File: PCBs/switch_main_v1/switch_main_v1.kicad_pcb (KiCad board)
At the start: 2 copper layers, 166 parts, among them IC1001 TJA1055T_3_2Z, J1101 76825-0004, J1102 PJ-002AH, J901 TMJG46945AENL, Q1101 DMTH6016LPSQ-13, U1101 TVS2701DRBR, U1102 MPQ5850GJ-AEC1-Z, U201 SJA1105QELY, U301 M24256X-FCU6T_VF, U302 STM32H573RIVx, U401 TPS16416DRCR, U402 LMR34206SC5QRNXRQ1, U403 LT8692SIV-PBF, U501 DP83867CSRGZR, U601 DP83867CSRGZR, U701 DP83867CSRGZR, U801 DP83867CSRGZR, Y501 ECS-250-18-36B2-CTY-TR, Y601 ECS-250-18-36B2-CTY-TR, Y701 ECS-250-18-36B2-CTY-TR, Y801 ECS-250-18-36B2-CTY-TR

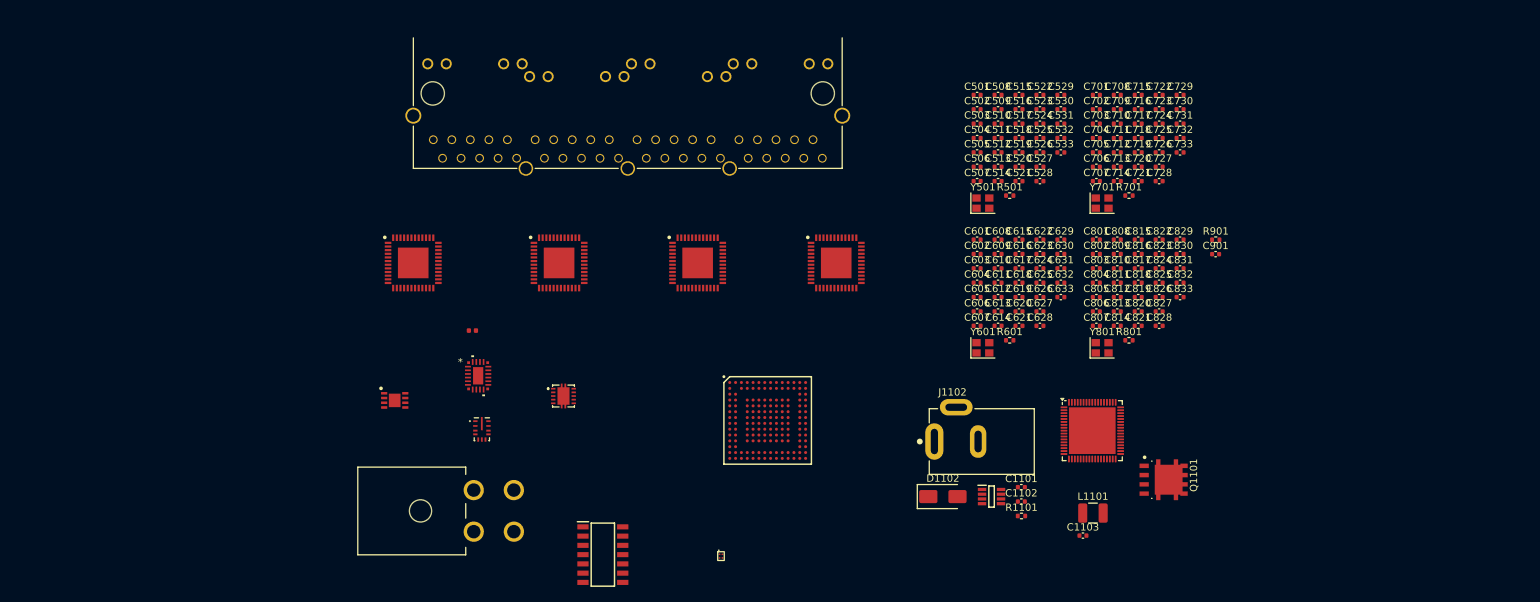
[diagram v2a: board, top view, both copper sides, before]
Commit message: GbE part of schematic done
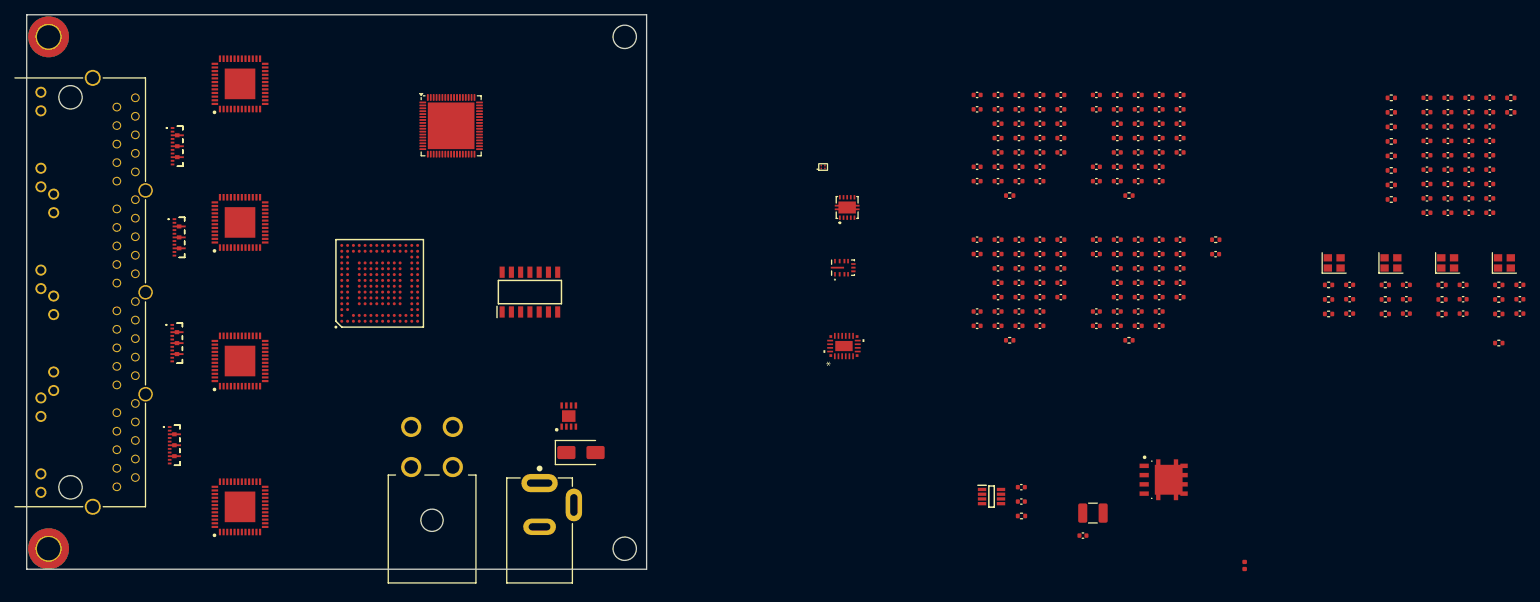
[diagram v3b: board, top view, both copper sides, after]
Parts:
- added C201: 100n, Capacitor_SMD:C_0402_1005Metric, F.Cu at (262.0, 66.4)
- added C202: 100n, Capacitor_SMD:C_0402_1005Metric, F.Cu at (262.0, 68.3)
- added C204: 100n, Capacitor_SMD:C_0402_1005Metric, F.Cu at (262.0, 70.3)
- added C205: 100n, Capacitor_SMD:C_0402_1005Metric, F.Cu at (262.0, 72.3)
- added C206: 100n, Capacitor_SMD:C_0402_1005Metric, F.Cu at (262.0, 74.2)
- added C207: 100n, Capacitor_SMD:C_0402_1005Metric, F.Cu at (262.0, 76.2)
- added C208: 100n, Capacitor_SMD:C_0402_1005Metric, F.Cu at (262.0, 78.2)
- added C209: 100n, Capacitor_SMD:C_0402_1005Metric, F.Cu at (262.0, 80.2)
- added C210: 100n, Capacitor_SMD:C_0402_1005Metric, F.Cu at (262.0, 82.1)
- added C211: 100n, Capacitor_SMD:C_0402_1005Metric, F.Cu at (264.9, 66.4)
- added C212: 100n, Capacitor_SMD:C_0402_1005Metric, F.Cu at (264.9, 68.3)
- added C213: 100n, Capacitor_SMD:C_0402_1005Metric, F.Cu at (264.9, 70.3)
- added C214: 1u, Capacitor_SMD:C_0402_1005Metric, F.Cu at (264.9, 72.3)
- added C215: 1u, Capacitor_SMD:C_0402_1005Metric, F.Cu at (264.9, 74.2)
- added C216: 100n, Capacitor_SMD:C_0402_1005Metric, F.Cu at (264.9, 76.2)
- added C217: 1u, Capacitor_SMD:C_0402_1005Metric, F.Cu at (264.9, 78.2)
- added C218: 1u, Capacitor_SMD:C_0402_1005Metric, F.Cu at (264.9, 80.2)
- added C219: 1u, Capacitor_SMD:C_0402_1005Metric, F.Cu at (264.9, 82.1)
- added C220: 100n, Capacitor_SMD:C_0402_1005Metric, F.Cu at (267.7, 66.4)
- added C221: 1u, Capacitor_SMD:C_0402_1005Metric, F.Cu at (267.7, 68.3)
- added C222: 10u, Capacitor_SMD:C_0402_1005Metric, F.Cu at (267.7, 70.3)
- added C224: 1u, Capacitor_SMD:C_0402_1005Metric, F.Cu at (267.7, 72.3)
- added C225: 1u, Capacitor_SMD:C_0402_1005Metric, F.Cu at (267.7, 74.2)
- added C227: 10u, Capacitor_SMD:C_0402_1005Metric, F.Cu at (267.7, 76.2)
- added C230: 10u, Capacitor_SMD:C_0402_1005Metric, F.Cu at (267.7, 78.2)
- added C231: 100p, Capacitor_SMD:C_0402_1005Metric, F.Cu at (267.7, 80.2)
- added C232: 100n, Capacitor_SMD:C_0402_1005Metric, F.Cu at (267.7, 82.1)
- added C233: 100n, Capacitor_SMD:C_0402_1005Metric, F.Cu at (270.6, 66.4)
- added C234: 100n, Capacitor_SMD:C_0402_1005Metric, F.Cu at (270.6, 68.3)
- added C235: 100n, Capacitor_SMD:C_0402_1005Metric, F.Cu at (270.6, 70.3)
- added C236: 100n, Capacitor_SMD:C_0402_1005Metric, F.Cu at (270.6, 72.3)
- added C237: 100n, Capacitor_SMD:C_0402_1005Metric, F.Cu at (270.6, 74.2)
- added C238: 1u, Capacitor_SMD:C_0402_1005Metric, F.Cu at (270.6, 76.2)
- added C239: 1u, Capacitor_SMD:C_0402_1005Metric, F.Cu at (270.6, 78.2)
- added C240: 100n, Capacitor_SMD:C_0402_1005Metric, F.Cu at (270.6, 80.2)
- added C241: 100n, Capacitor_SMD:C_0402_1005Metric, F.Cu at (270.6, 82.1)
- added D901: ESD8708MUTAG, switch_footprints:ESD8708MUTAG, F.Cu at (90.7, 73.0)
- added D902: ESD8708MUTAG, switch_footprints:ESD8708MUTAG, F.Cu at (90.9, 85.5)
- added D903: ESD8708MUTAG, switch_footprints:ESD8708MUTAG, F.Cu at (90.6, 100.0)
- added D904: ESD8708MUTAG, switch_footprints:ESD8708MUTAG, F.Cu at (90.3, 114.0)
- added H101: MountingHole_Pad, MountingHole:MountingHole_3.2mm_M3_DIN965_Pad_TopBottom, F.Cu at (73.0, 128.2)
- added H102: MountingHole_Pad, MountingHole:MountingHole_3.2mm_M3_DIN965_Pad_TopBottom, F.Cu at (73.0, 58.0)
- added H103: MountingHole, MountingHole:MountingHole_3.2mm_M3_DIN965, F.Cu at (152.0, 58.0)
- added H104: MountingHole, MountingHole:MountingHole_3.2mm_M3_DIN965, F.Cu at (152.0, 128.2)
- added R201: 1k, Resistor_SMD:R_0402_1005Metric, F.Cu at (273.5, 66.4)
- added R202: 2k2, Resistor_SMD:R_0402_1005Metric, F.Cu at (273.5, 68.4)
- added R301: 1k5, Resistor_SMD:R_0402_1005Metric, F.Cu at (271.9, 100.0)
- added R502: 27k, Resistor_SMD:R_0402_1005Metric, F.Cu at (248.5, 92.0)
- added R503: 2k2, Resistor_SMD:R_0402_1005Metric, F.Cu at (248.5, 94.0)
- added R504: 2k2, Resistor_SMD:R_0402_1005Metric, F.Cu at (248.5, 96.0)
- added R602: 27k, Resistor_SMD:R_0402_1005Metric, F.Cu at (256.3, 92.0)
- added R603: 2k2, Resistor_SMD:R_0402_1005Metric, F.Cu at (256.3, 94.0)
- added R604: 2k2, Resistor_SMD:R_0402_1005Metric, F.Cu at (256.3, 96.0)
- added R702: 27k, Resistor_SMD:R_0402_1005Metric, F.Cu at (264.1, 92.0)
- added R703: 2k2, Resistor_SMD:R_0402_1005Metric, F.Cu at (264.1, 94.0)
- added R704: 2k2, Resistor_SMD:R_0402_1005Metric, F.Cu at (264.1, 96.0)
- added R802: 27k, Resistor_SMD:R_0402_1005Metric, F.Cu at (271.9, 92.0)
- added R803: 2k2, Resistor_SMD:R_0402_1005Metric, F.Cu at (271.9, 94.0)
- added R804: 2k2, Resistor_SMD:R_0402_1005Metric, F.Cu at (271.9, 96.0)
- added R902: 470R, Resistor_SMD:R_0402_1005Metric, F.Cu at (257.1, 66.4)
- added R903: 470R, Resistor_SMD:R_0402_1005Metric, F.Cu at (257.1, 68.4)
- added R904: 470R, Resistor_SMD:R_0402_1005Metric, F.Cu at (257.1, 70.3)
- added R905: 470R, Resistor_SMD:R_0402_1005Metric, F.Cu at (257.1, 72.3)
- added R906: 470R, Resistor_SMD:R_0402_1005Metric, F.Cu at (257.1, 74.3)
- added R907: 470R, Resistor_SMD:R_0402_1005Metric, F.Cu at (257.1, 76.3)
- added R908: 470R, Resistor_SMD:R_0402_1005Metric, F.Cu at (257.1, 78.3)
- added R909: 470R, Resistor_SMD:R_0402_1005Metric, F.Cu at (257.1, 80.3)
- C901: value C_Small -> 4n7
- R901: value R_Small -> 1M
- moved D1101 110.7 mm to (237.0, 130.5), turned to 90 degrees
- moved U302 97.3 mm to (128.2, 70.2)
- moved U801 85.4 mm to (99.2, 64.5), turned to 90 degrees
- moved J901 73.0 mm to (82.5, 93.0), turned to -90 degrees
- moved U601 63.0 mm to (99.2, 83.5), turned to 90 degrees
- moved C603 58.9 mm to (259.2, 92.0)
- moved C604 58.9 mm to (259.2, 94.0)
- moved C605 58.9 mm to (259.2, 96.0)
- moved C803 58.1 mm to (274.7, 92.0)
- moved C804 58.1 mm to (274.7, 94.0)
- moved C805 58.1 mm to (274.7, 96.0)
- moved Y601 57.1 mm to (257.1, 89.0)
- moved U201 56.4 mm to (118.4, 91.8), turned to 90 degrees
- moved Y801 56.4 mm to (272.6, 89.0)
- moved C503 55.7 mm to (251.4, 92.0)
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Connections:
- net /Switch/SPI.CS renamed /SPI3.CS
- net /Switch/SPI.MISO renamed /SPI3.MISO
- net /Switch/SPI.MOSI renamed /SPI3.MOSI
- net /Switch/SPI.SCK renamed /SPI3.SCK
- C503 pad 2: /PHY_1_CLK -> GND
- C504 pad 1: /PHY 1/XI -> /PHY 1/XO
- C505 pad 1: /PHY 1/XO -> /PHY 1/XI
- C505 pad 2: GND -> /PHY_1_CLK
- C603 pad 2: /PHY_2_CLK -> GND
- C604 pad 1: /PHY 2/XI -> /PHY 2/XO
- C605 pad 1: /PHY 2/XO -> /PHY 2/XI
- C605 pad 2: GND -> /PHY_2_CLK
- C703 pad 2: /PHY_3_CLK -> GND
- C704 pad 1: /PHY 3/XI -> /PHY 3/XO
- C705 pad 1: /PHY 3/XO -> /PHY 3/XI
- C705 pad 2: GND -> /PHY_3_CLK
- C803 pad 2: /PHY_4_CLK -> GND
- C804 pad 1: /PHY 4/XI -> /PHY 4/XO
- C805 pad 1: /PHY 4/XO -> /PHY 4/XI
- C805 pad 2: GND -> /PHY_4_CLK
- J901 pad 11A: unconnected-(J901-ANODE-Pad11A) -> /RJ45s/LED_G_1_A
- J901 pad 11B: unconnected-(J901-ANODE-Pad11B) -> /RJ45s/LED_G_2_A
- J901 pad 11C: unconnected-(J901-ANODE-Pad11C) -> /RJ45s/LED_G_3_A
- J901 pad 11D: unconnected-(J901-ANODE-Pad11D) -> /RJ45s/LED_G_4_A
- J901 pad 12A: unconnected-(J901-CATHODE-Pad12A) -> GND
- J901 pad 12B: unconnected-(J901-CATHODE-Pad12B) -> GND
- J901 pad 12C: unconnected-(J901-CATHODE-Pad12C) -> GND
- J901 pad 12D: unconnected-(J901-CATHODE-Pad12D) -> GND
- J901 pad 13A: unconnected-(J901-ANODE-Pad13A) -> /RJ45s/LED_Y_1_A
- J901 pad 13B: unconnected-(J901-ANODE-Pad13B) -> /RJ45s/LED_Y_2_A
- J901 pad 13C: unconnected-(J901-ANODE-Pad13C) -> /RJ45s/LED_Y_3_A
- J901 pad 13D: unconnected-(J901-ANODE-Pad13D) -> /RJ45s/LED_Y_4_A
- J901 pad 14A: unconnected-(J901-CATHODE-Pad14A) -> GND
- J901 pad 14B: unconnected-(J901-CATHODE-Pad14B) -> GND
- J901 pad 14C: unconnected-(J901-CATHODE-Pad14C) -> GND
- J901 pad 14D: unconnected-(J901-CATHODE-Pad14D) -> GND
- U201 pad J1: unconnected-(U201B-VDDA_PLL-PadJ1) -> +1V2
- U201 pad K1: unconnected-(U201B-VDDA_OSC-PadK1) -> +1V2
- U201 pad K2: unconnected-(U201A-OSC_IN-PadK2) -> /Switch/OSC_IN
- U201 pad P3: /Switch/RST -> /ETHERNET_RST
- U501 pad 20: unconnected-(U501-JTAG_CLK-Pad20) -> GND
- U501 pad 22: unconnected-(U501-JTAG_TMS-Pad22) -> +2V5
- U501 pad 23: unconnected-(U501-JTAG_TDI-Pad23) -> +2V5
- U501 pad 43: unconnected-(U501-RESET_N-Pad43) -> /ETHERNET_RST
- U501 pad 44: unconnected-(U501-INT/PWDN-Pad44) -> /PHY_INT
- U501 pad 45: unconnected-(U501-LED_2-Pad45) -> /LED_Y_1
- U501 pad 47: unconnected-(U501-LED_0-Pad47) -> /LED_G_1
- U601 pad 20: unconnected-(U601-JTAG_CLK-Pad20) -> GND
- U601 pad 22: unconnected-(U601-JTAG_TMS-Pad22) -> +2V5
- U601 pad 23: unconnected-(U601-JTAG_TDI-Pad23) -> +2V5
- U601 pad 43: unconnected-(U601-RESET_N-Pad43) -> /ETHERNET_RST
- U601 pad 44: unconnected-(U601-INT/PWDN-Pad44) -> /PHY_INT
- U601 pad 45: unconnected-(U601-LED_2-Pad45) -> /LED_Y_2
- U601 pad 47: unconnected-(U601-LED_0-Pad47) -> /LED_G_2
- U701 pad 20: unconnected-(U701-JTAG_CLK-Pad20) -> GND
- U701 pad 22: unconnected-(U701-JTAG_TMS-Pad22) -> +2V5
- U701 pad 23: unconnected-(U701-JTAG_TDI-Pad23) -> +2V5
- U701 pad 43: unconnected-(U701-RESET_N-Pad43) -> /ETHERNET_RST
- U701 pad 44: unconnected-(U701-INT/PWDN-Pad44) -> /PHY_INT
- U701 pad 45: unconnected-(U701-LED_2-Pad45) -> /LED_Y_3
- U701 pad 47: unconnected-(U701-LED_0-Pad47) -> /LED_G_3
- U801 pad 20: unconnected-(U801-JTAG_CLK-Pad20) -> GND
- U801 pad 22: unconnected-(U801-JTAG_TMS-Pad22) -> +2V5
- U801 pad 23: unconnected-(U801-JTAG_TDI-Pad23) -> +2V5
- U801 pad 43: unconnected-(U801-RESET_N-Pad43) -> /ETHERNET_RST
- U801 pad 44: unconnected-(U801-INT/PWDN-Pad44) -> /PHY_INT
- U801 pad 45: unconnected-(U801-LED_2-Pad45) -> /LED_Y_4
- U801 pad 47: unconnected-(U801-LED_0-Pad47) -> /LED_G_4
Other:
- board outline added: 85 x 76 mm

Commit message: Changed MCU to STM32H573IIK3Q
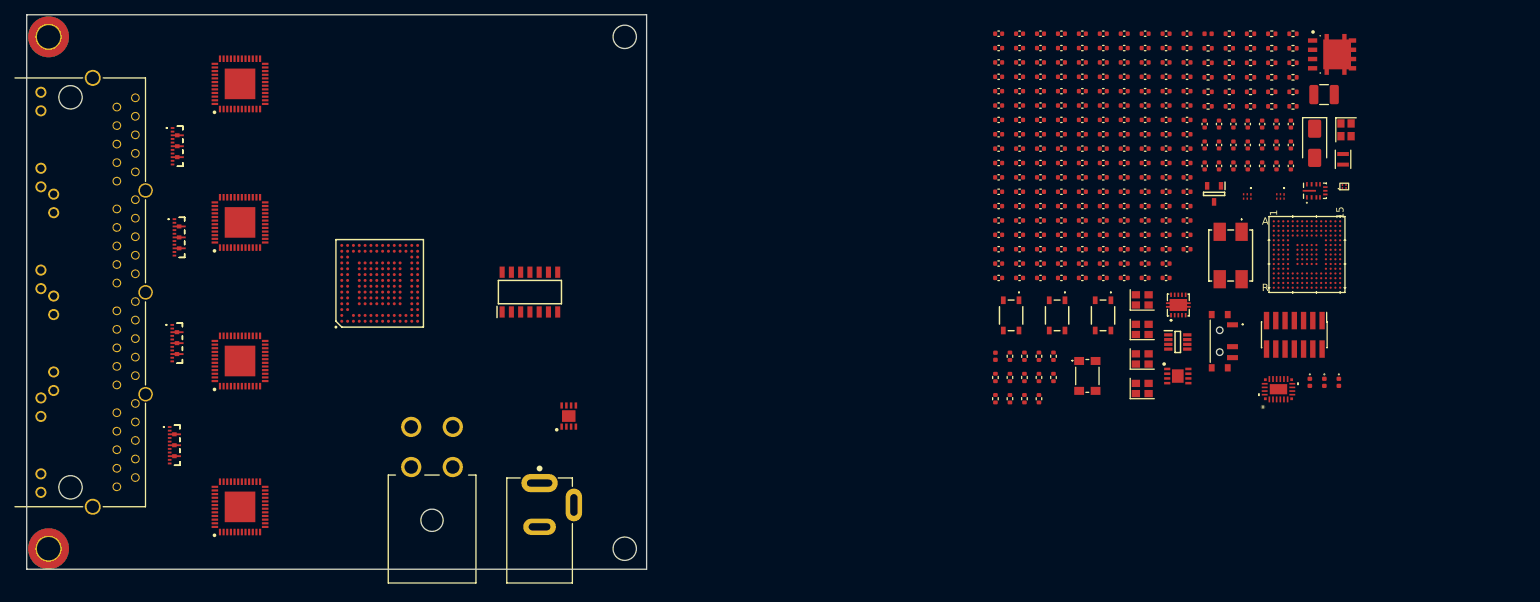
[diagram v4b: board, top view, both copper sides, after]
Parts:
- added C301: 220p, Capacitor_SMD:C_0402_1005Metric, F.Cu at (231.5, 70.0)
- added C302: 100n, Capacitor_SMD:C_0402_1005Metric, F.Cu at (233.5, 70.0)
- added C303: 1u, Capacitor_SMD:C_0402_1005Metric, F.Cu at (235.5, 70.0)
- added C304: 4u7, Capacitor_SMD:C_0402_1005Metric, F.Cu at (237.4, 70.0)
- added C305: 10u, Capacitor_SMD:C_0402_1005Metric, F.Cu at (239.4, 70.0)
- added C306: 100n, Capacitor_SMD:C_0402_1005Metric, F.Cu at (241.4, 70.0)
- added C307: 10n, Capacitor_SMD:C_0402_1005Metric, F.Cu at (243.3, 70.0)
- added C308: 10n, Capacitor_SMD:C_0402_1005Metric, F.Cu at (231.5, 72.8)
- added C309: 4u7, Capacitor_SMD:C_0402_1005Metric, F.Cu at (233.5, 72.8)
- added C310: 100n, Capacitor_SMD:C_0402_1005Metric, F.Cu at (235.5, 72.8)
- added C311: 10n, Capacitor_SMD:C_0402_1005Metric, F.Cu at (237.4, 72.8)
- added C312: 6p, Capacitor_SMD:C_0402_1005Metric, F.Cu at (239.4, 72.8)
- added C313: 4u7, Capacitor_SMD:C_0402_1005Metric, F.Cu at (241.4, 72.8)
- added C314: 100n, Capacitor_SMD:C_0402_1005Metric, F.Cu at (243.3, 72.8)
- added C315: 6p, Capacitor_SMD:C_0402_1005Metric, F.Cu at (231.5, 75.7)
- added C316: 100n, Capacitor_SMD:C_0402_1005Metric, F.Cu at (209.0, 57.6)
- added C317: 100n, Capacitor_SMD:C_0402_1005Metric, F.Cu at (233.5, 75.7)
- added C318: 100n, Capacitor_SMD:C_0402_1005Metric, F.Cu at (235.5, 75.7)
- added C319: 100n, Capacitor_SMD:C_0402_1005Metric, F.Cu at (209.0, 59.5)
- added C320: 100n, Capacitor_SMD:C_0402_1005Metric, F.Cu at (209.0, 61.5)
- added C321: 1u, Capacitor_SMD:C_0402_1005Metric, F.Cu at (237.4, 75.7)
- added C322: 100n, Capacitor_SMD:C_0402_1005Metric, F.Cu at (239.4, 75.7)
- added C323: 100n, Capacitor_SMD:C_0402_1005Metric, F.Cu at (209.0, 63.5)
- added C324: 100n, Capacitor_SMD:C_0402_1005Metric, F.Cu at (209.0, 65.5)
- added C325: 100n, Capacitor_SMD:C_0402_1005Metric, F.Cu at (209.0, 67.4)
- added C326: 100n, Capacitor_SMD:C_0402_1005Metric, F.Cu at (241.4, 75.7)
- added C330: 4u7, Capacitor_SMD:C_0402_1005Metric, F.Cu at (243.3, 75.7)
- added D1001: PESD2CANFD24V-TR, switch_footprints:SOT95P230X110-3N, F.Cu at (232.8, 79.5)
- added D1103: AXGD10402KR, switch_footprints:DIONM105X51N, F.Cu at (232.0, 57.6)
- added D301: Red, LED_SMD:LED_0402_1005Metric, F.Cu at (245.9, 105.4)
- added D302: Green, LED_SMD:LED_0402_1005Metric, F.Cu at (247.9, 105.4)
- added D303: Blue, LED_SMD:LED_0402_1005Metric, F.Cu at (249.9, 105.4)
- added FL1101: SRF7035A-301Y, switch_footprints:SRF7035A301Y, F.Cu at (235.1, 88.0)
- added J1104: STDC, switch_footprints:STDC14, F.Cu at (243.8, 98.9)
- added L1001: SRF4532-110Y, switch_footprints:SRF4532101Y, F.Cu at (215.2, 104.5)
- added L301: 2u2, Inductor_SMD:L_Murata_DFE201610P, F.Cu at (250.5, 74.8)
- added R1001: 100k, Resistor_SMD:R_0402_1005Metric, F.Cu at (210.8, 104.7)
- added R1002: 100k, Resistor_SMD:R_0402_1005Metric, F.Cu at (202.8, 107.6)
- added R1003: 100k, Resistor_SMD:R_0402_1005Metric, F.Cu at (204.8, 107.6)
- added R1004: 10k, Resistor_SMD:R_0402_1005Metric, F.Cu at (206.8, 107.6)
- added R1005: 10k, Resistor_SMD:R_0402_1005Metric, F.Cu at (208.8, 107.6)
- added R302: 10k, Resistor_SMD:R_0402_1005Metric, F.Cu at (204.8, 101.8)
- added R303: 10k, Resistor_SMD:R_0402_1005Metric, F.Cu at (206.8, 101.8)
- added R304: 100k, Resistor_SMD:R_0402_1005Metric, F.Cu at (208.8, 101.8)
- added R305: 4k7, Resistor_SMD:R_0402_1005Metric, F.Cu at (210.8, 101.8)
- added R306: 2k7, Resistor_SMD:R_0402_1005Metric, F.Cu at (202.8, 104.7)
- added R307: 2k7, Resistor_SMD:R_0402_1005Metric, F.Cu at (204.8, 104.7)
- added R308: 2k7, Resistor_SMD:R_0402_1005Metric, F.Cu at (206.8, 104.7)
- added R309: 1k, Resistor_SMD:R_0402_1005Metric, F.Cu at (208.8, 104.7)
- added S301: TS20-42-25-WT-160-SMT-TR, switch_footprints:TS204225WT160SMTTRMSL, F.Cu at (205.0, 96.2)
- added S302: TS20-42-25-WT-160-SMT-TR, switch_footprints:TS204225WT160SMTTRMSL, F.Cu at (211.3, 96.2)
- added S303: TS20-42-25-WT-160-SMT-TR, switch_footprints:TS204225WT160SMTTRMSL, F.Cu at (217.6, 96.2)
- added S305: PCM12SMTR, switch_footprints:PCM12SMTR, F.Cu at (233.6, 99.7)
- added U1103: TPD4S012DRYR, switch_footprints:TPD4S012DRYR, F.Cu at (237.4, 79.9)
- added U1104: TPD4S012DRYR, switch_footprints:TPD4S012DRYR, F.Cu at (241.9, 79.9)
- added U1105: TVS2701DRBR, switch_footprints:SON65P300X300X100-9N-D, F.Cu at (227.8, 104.5)
- added Y301: ECS-250-10-36Q-AES-TR, Crystal:Crystal_SMD_2520-4Pin_2.5x2.0mm, F.Cu at (250.9, 70.8)
- U302: value STM32H573RIVx -> STM32H573IIK3Q; footprint switch_footprints:QFN-68-1EP_8x8mm_P0.4mm_EP6.4x6.4mm -> switch_footprints:STM32H573IIK3Q
- U501, U601, U701, U801: value DP83867CSRGZR -> DP83867ISRGZR
- moved U302 118.7 mm to (245.5, 87.8)
- moved D1102 109.2 mm to (246.6, 72.6), turned to -90 degrees
- moved U301 71.5 mm to (250.7, 78.5)
- moved R1101 67.4 mm to (243.6, 67.5)
- moved U402 65.6 mm to (246.7, 79.1)
- moved L1101 65.5 mm to (247.9, 65.9)
- moved C233 65.1 mm to (206.1, 75.3)
- moved C234 65.1 mm to (206.1, 77.3)
- moved C235 65.1 mm to (206.1, 79.2)
- moved C236 65.1 mm to (206.1, 81.2)
- moved C237 65.1 mm to (206.1, 83.2)
- moved C238 65.1 mm to (206.1, 85.2)
- moved C239 65.1 mm to (206.1, 87.1)
- moved C240 65.1 mm to (206.1, 89.1)
- moved C241 65.1 mm to (206.1, 91.1)
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- renumbered IC1001 to U1001
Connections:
- net /Connectors/CAN.CANH renamed /FTCAN.CANH
- net /Connectors/CAN.CANL renamed /FTCAN.CANL
- net Net-(Q1101-G) renamed /Connectors/GATE
- net Net-(U1102-EN/UVLO) renamed /Connectors/EN
- net Net-(U1102-RES) renamed /Connectors/RES
- net Net-(U1102-SW) renamed /Connectors/SW
- C1101 pad 1: Net-(Q1101-D) -> /Connectors/VIN_PROTECTED
- C1102 pad 1: Net-(Q1101-D) -> /Connectors/VIN_PROTECTED
- C1103 pad 1: /Connectors/VIN_RAW -> /Connectors/VIN_FILTERED
- D1101 pad 1: GND -> /Connectors/GND_RAW
- D1102 pad 1: /Connectors/VIN_RAW -> /Connectors/VIN_FILTERED
- J1101 pad 4: GND -> /Connectors/GND_RAW
- L1101 pad 1: Net-(Q1101-D) -> /Connectors/VIN_PROTECTED
- Q1101 pad 1: /Connectors/VIN_RAW -> /Connectors/VIN_FILTERED
- Q1101 pad 2: /Connectors/VIN_RAW -> /Connectors/VIN_FILTERED
- Q1101 pad 3: /Connectors/VIN_RAW -> /Connectors/VIN_FILTERED
- Q1101 pad 5-6-7-8: Net-(Q1101-D) -> /Connectors/VIN_PROTECTED
- R1101 pad 1: /Connectors/VIN_RAW -> /Connectors/VIN_FILTERED
- U1001 pad 1: unconnected-(IC1001-INH-Pad1) -> /5V0_EN
- U1001 pad 10: unconnected-(IC1001-VCC-Pad10) -> +5V
- U1001 pad 11: unconnected-(IC1001-CANH-Pad11) -> /CAN/CANH
- U1001 pad 12: unconnected-(IC1001-CANL-Pad12) -> /CAN/CANL
- U1001 pad 13: unconnected-(IC1001-GND-Pad13) -> GND
- U1001 pad 14: unconnected-(IC1001-BAT-Pad14) -> +VIN
- U1001 pad 2: unconnected-(IC1001-TXD-Pad2) -> /CAN.TXD
- U1001 pad 3: unconnected-(IC1001-RXD-Pad3) -> /CAN.RXD
- U1001 pad 4: unconnected-(IC1001-~{ERR}-Pad4) -> /CAN/CAN_ERR
- U1001 pad 8: unconnected-(IC1001-RTH-Pad8) -> /CAN/RTH
- U1001 pad 9: unconnected-(IC1001-RTL-Pad9) -> /CAN/RTL
- U1101 pad 5: GND -> /Connectors/GND_RAW
- U1101 pad 6: GND -> /Connectors/GND_RAW
- U1101 pad 7: GND -> /Connectors/GND_RAW
- U1101 pad 8: GND -> /Connectors/GND_RAW
- U1102 pad 6: Net-(Q1101-D) -> /Connectors/VIN_PROTECTED
- U1102 pad 8: /Connectors/VIN_RAW -> /Connectors/VIN_FILTERED
- U301 pad A1: unconnected-(U301-VCC-PadA1) -> +2V5
- U301 pad A2: unconnected-(U301-SCL-PadA2) -> /MCU/I2C4_SCL
- U301 pad B1: unconnected-(U301-SDA-PadB1) -> /MCU/I2C4_SDA
- U301 pad B2: unconnected-(U301-VSS-PadB2) -> GND
- U401 pad 1: unconnected-(U401-IN-Pad1) -> /Connectors/VIN_PROTECTED
- U401 pad 10: unconnected-(U401-OUT-Pad10) -> +VIN
- U401 pad 2: unconnected-(U401-VCC-Pad2) -> /Connectors/VIN_PROTECTED
- U402 pad 10: unconnected-(U402-VIN-Pad10) -> Net-(U402-VIN-Pad10)
- U402 pad 2: unconnected-(U402-VIN-Pad2) -> Net-(U402-VIN-Pad10)
- U402 pad 9: /Power/5V0_EN -> /5V0_EN
- U403 pad 1: unconnected-(U403-VIN1-Pad1) -> +VIN
- U403 pad 10: unconnected-(U403-FB4-Pad10) -> Net-(U403-FB4)
- U403 pad 13: unconnected-(U403-SW4-Pad13) -> Net-(U403-SW4)
- U403 pad 14: unconnected-(U403-SW3-Pad14) -> Net-(U403-SW3)
- U403 pad 15: unconnected-(U403-SW2-Pad15) -> Net-(U403-SW2)
- U403 pad 16: unconnected-(U403-VIN234-Pad16) -> Net-(U403-EN2)
- U403 pad 17: unconnected-(U403-SW1-Pad17) -> Net-(U403-SW1)
- U403 pad 2: unconnected-(U403-EN/UVLO-Pad2) -> +VIN
- U403 pad 3: unconnected-(U403-EN1-Pad3) -> +VIN
- U403 pad 4: unconnected-(U403-EN4-Pad4) -> Net-(U403-EN2)
- U403 pad 5: unconnected-(U403-EN3-Pad5) -> Net-(U403-EN2)
- U403 pad 6: unconnected-(U403-EN2-Pad6) -> Net-(U403-EN2)
- U403 pad 7: unconnected-(U403-FB1-Pad7) -> Net-(U403-EN2)
- U403 pad 8: unconnected-(U403-FB2-Pad8) -> Net-(U403-FB2)
- U403 pad 9: unconnected-(U403-FB3-Pad9) -> Net-(U403-FB3)
